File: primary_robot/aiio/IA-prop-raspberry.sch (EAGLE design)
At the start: 60 parts, among them U1 ARDUINO_R3_SHIELD

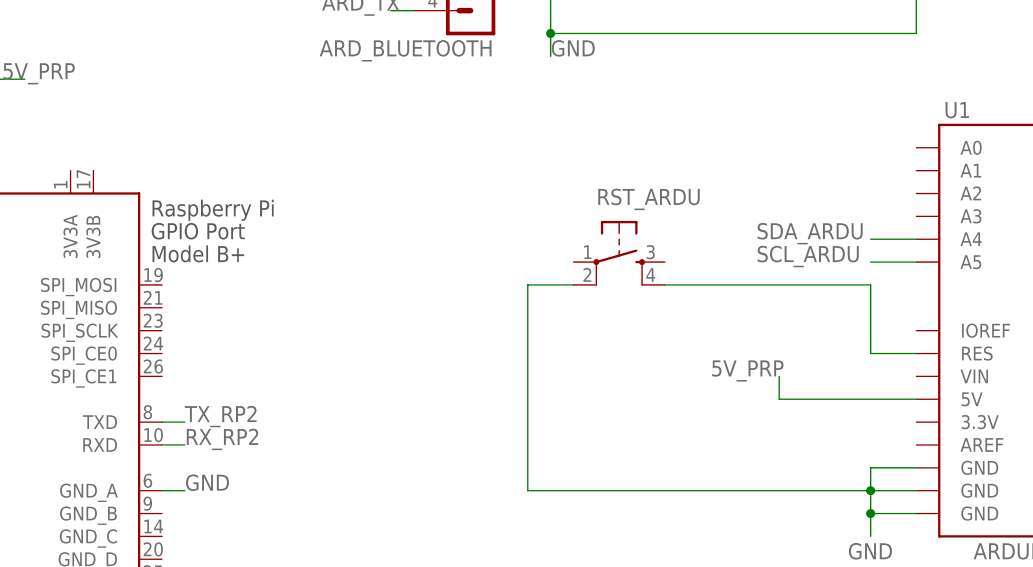
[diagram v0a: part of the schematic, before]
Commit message: [AIIO] Adds a reset button for the Raspi
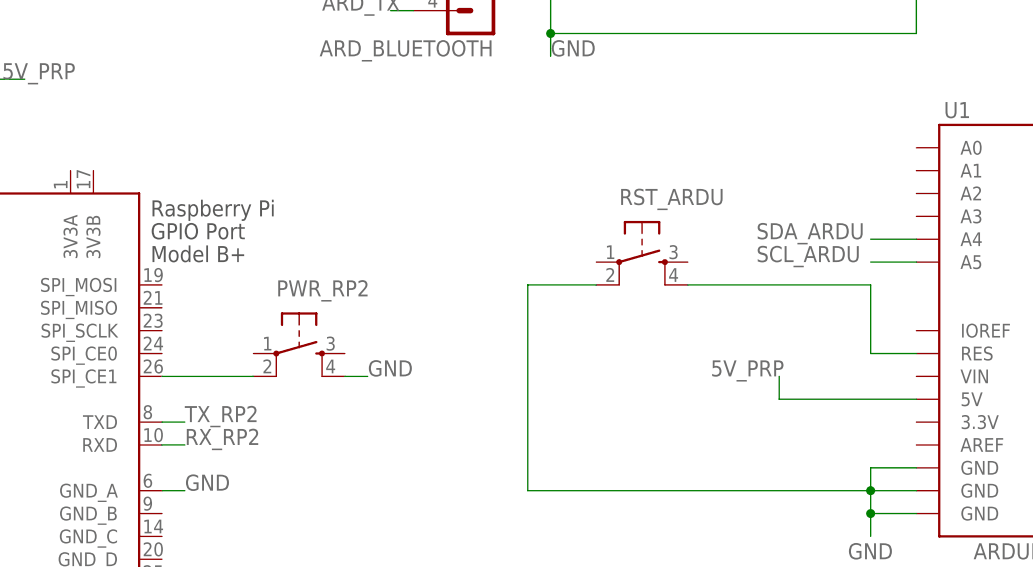
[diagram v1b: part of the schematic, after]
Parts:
- added PWR_RP2: (no value), SparkFun:TAC_SWITCHPTH
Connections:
- new net RP2_PWR: PWR_RP2.2, RP2.SPI_CE1
- net GND: now also PWR_RP2.4
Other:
- moved on the sheet: RST_ARDU
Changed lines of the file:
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@@
 <part name="R17" library="SparkFun" deviceset="RESISTOR" device="AXIAL-0.3" value="10K"/>
 <part name="R18" library="SparkFun" deviceset="RESISTOR" device="AXIAL-0.3" value="10K"/>
+<part name="PWR_RP2" library="SparkFun" deviceset="TAC_SWITCH" device="PTH"/>
 </parts>
 <sheets>
@@
 <instance part="LED1" gate="G$1" x="91.44" y="-83.82" rot="R180"/>
 <instance part="R3" gate="G$1" x="91.44" y="-71.12" rot="R90"/>
-<instance part="RST_ARDU" gate="S" x="165.1" y="-111.76"/>
+<instance part="RST_ARDU" gate="S" x="167.64" y="-111.76"/>
 <instance part="5V_SAL" gate="-1" x="-58.42" y="60.96"/>
 <instance part="5V_SAL" gate="-2" x="-58.42" y="55.88"/>
@@
 <instance part="R17" gate="G$1" x="-12.7" y="-63.5" rot="R90"/>
 <instance part="R18" gate="G$1" x="-12.7" y="-81.28" rot="R90"/>
+<instance part="PWR_RP2" gate="S" x="129.54" y="-121.92"/>
 </instances>
 <busses>
@@
 <label x="190.5" y="-144.78" size="1.778" layer="95"/>
 <pinref part="RST_ARDU" gate="S" pin="2"/>
-<wire x1="160.02" y1="-114.3" x2="154.94" y2="-114.3" width="0.1524" layer="91"/>
+<wire x1="162.56" y1="-114.3" x2="154.94" y2="-114.3" width="0.1524" layer="91"/>
 <wire x1="154.94" y1="-114.3" x2="154.94" y2="-137.16" width="0.1524" layer="91"/>
 <wire x1="154.94" y1="-137.16" x2="193.04" y2="-137.16" width="0.1524" layer="91"/>
@@
 <junction x="91.44" y="10.16"/>
 <label x="91.44" y="-2.54" size="1.778" layer="95"/>
+</segment>
+<segment>
+<pinref part="PWR_RP2" gate="S" pin="4"/>
+<wire x1="134.62" y1="-124.46" x2="137.16" y2="-124.46" width="0.1524" layer="91"/>
+<label x="137.16" y="-124.46" size="1.778" layer="95"/>
 </segment>
 </net>
@@
 <wire x1="198.12" y1="-121.92" x2="193.04" y2="-121.92" width="0.1524" layer="91"/>
 <pinref part="RST_ARDU" gate="S" pin="4"/>
-<wire x1="170.18" y1="-114.3" x2="193.04" y2="-114.3" width="0.1524" layer="91"/>
+<wire x1="172.72" y1="-114.3" x2="193.04" y2="-114.3" width="0.1524" layer="91"/>
 <wire x1="193.04" y1="-114.3" x2="193.04" y2="-121.92" width="0.1524" layer="91"/>
 </segment>
@@
 </segment>
 </net>
+<net name="RP2_PWR" class="0">
+<segment>
+<pinref part="RP2" gate="G$1" pin="SPI_CE1"/>
+<pinref part="PWR_RP2" gate="S" pin="2"/>
+<wire x1="114.3" y1="-124.46" x2="124.46" y2="-124.46" width="0.1524" layer="91"/>
+</segment>
+</net>

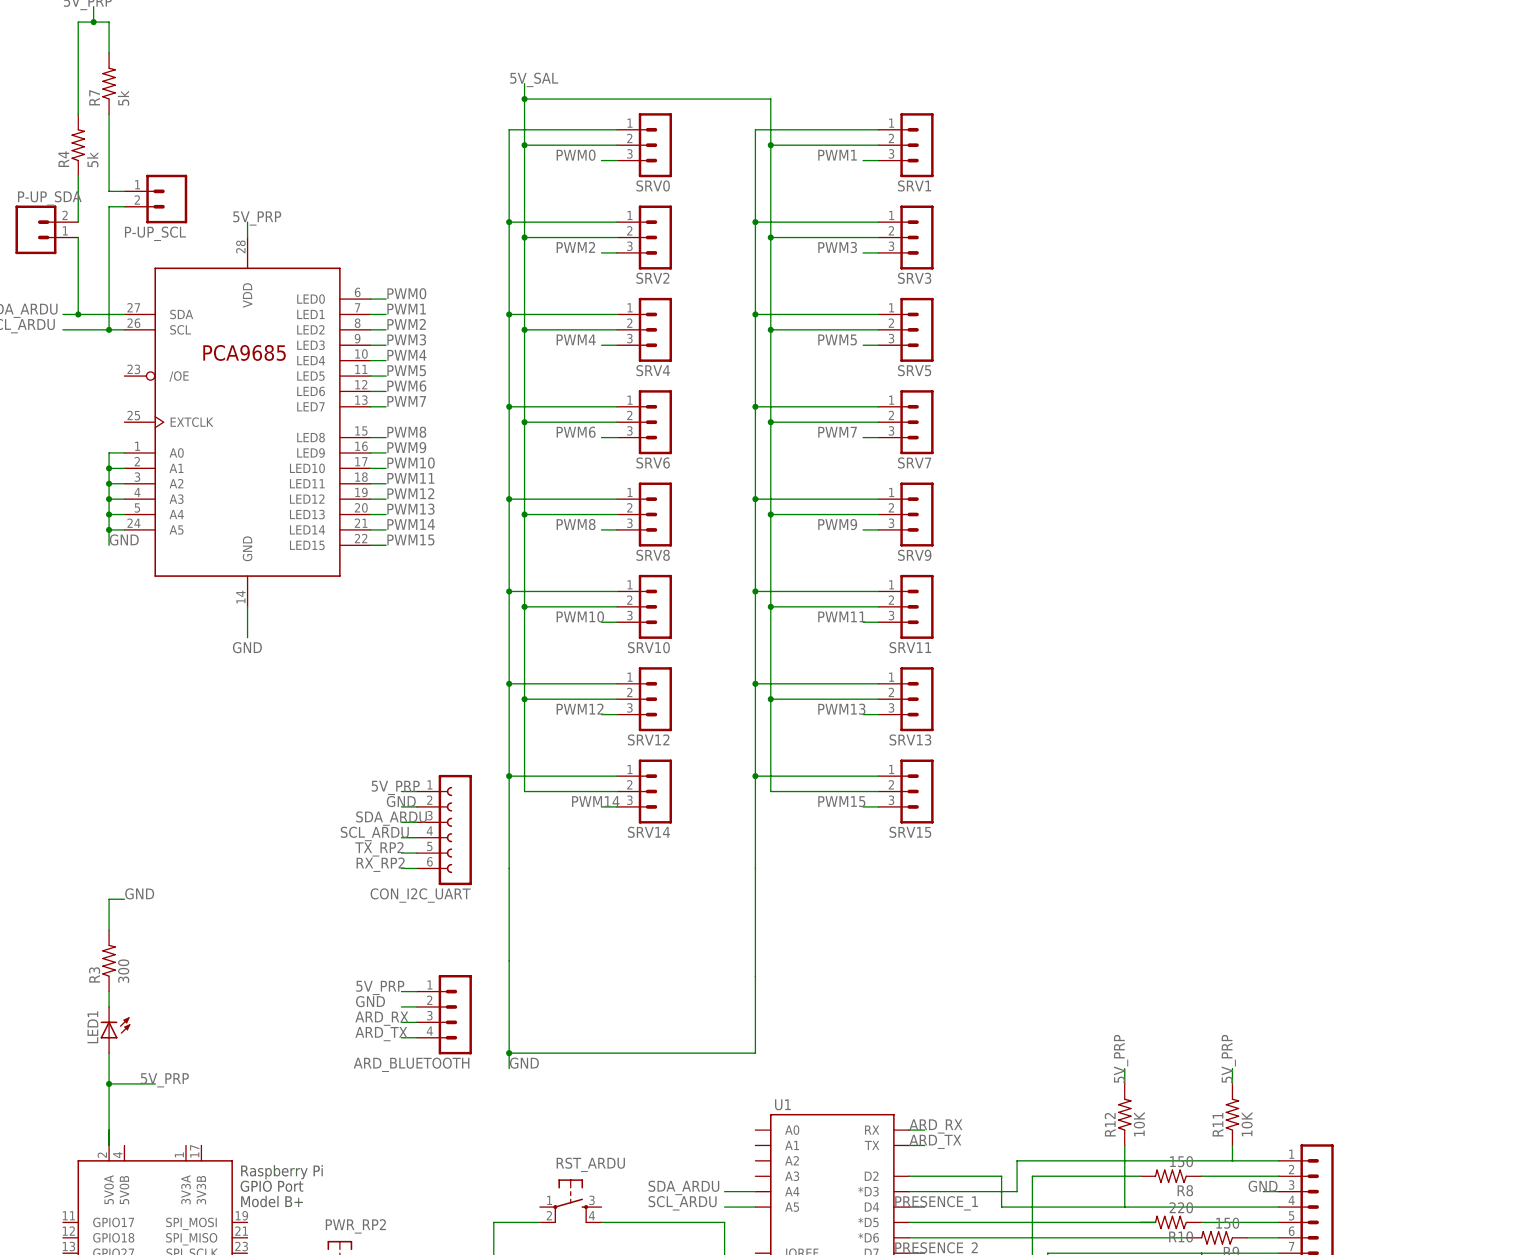
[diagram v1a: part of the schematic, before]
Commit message: [AIIO_board] Add I2C bus "I2C0" for sonar sensors on shematic file.
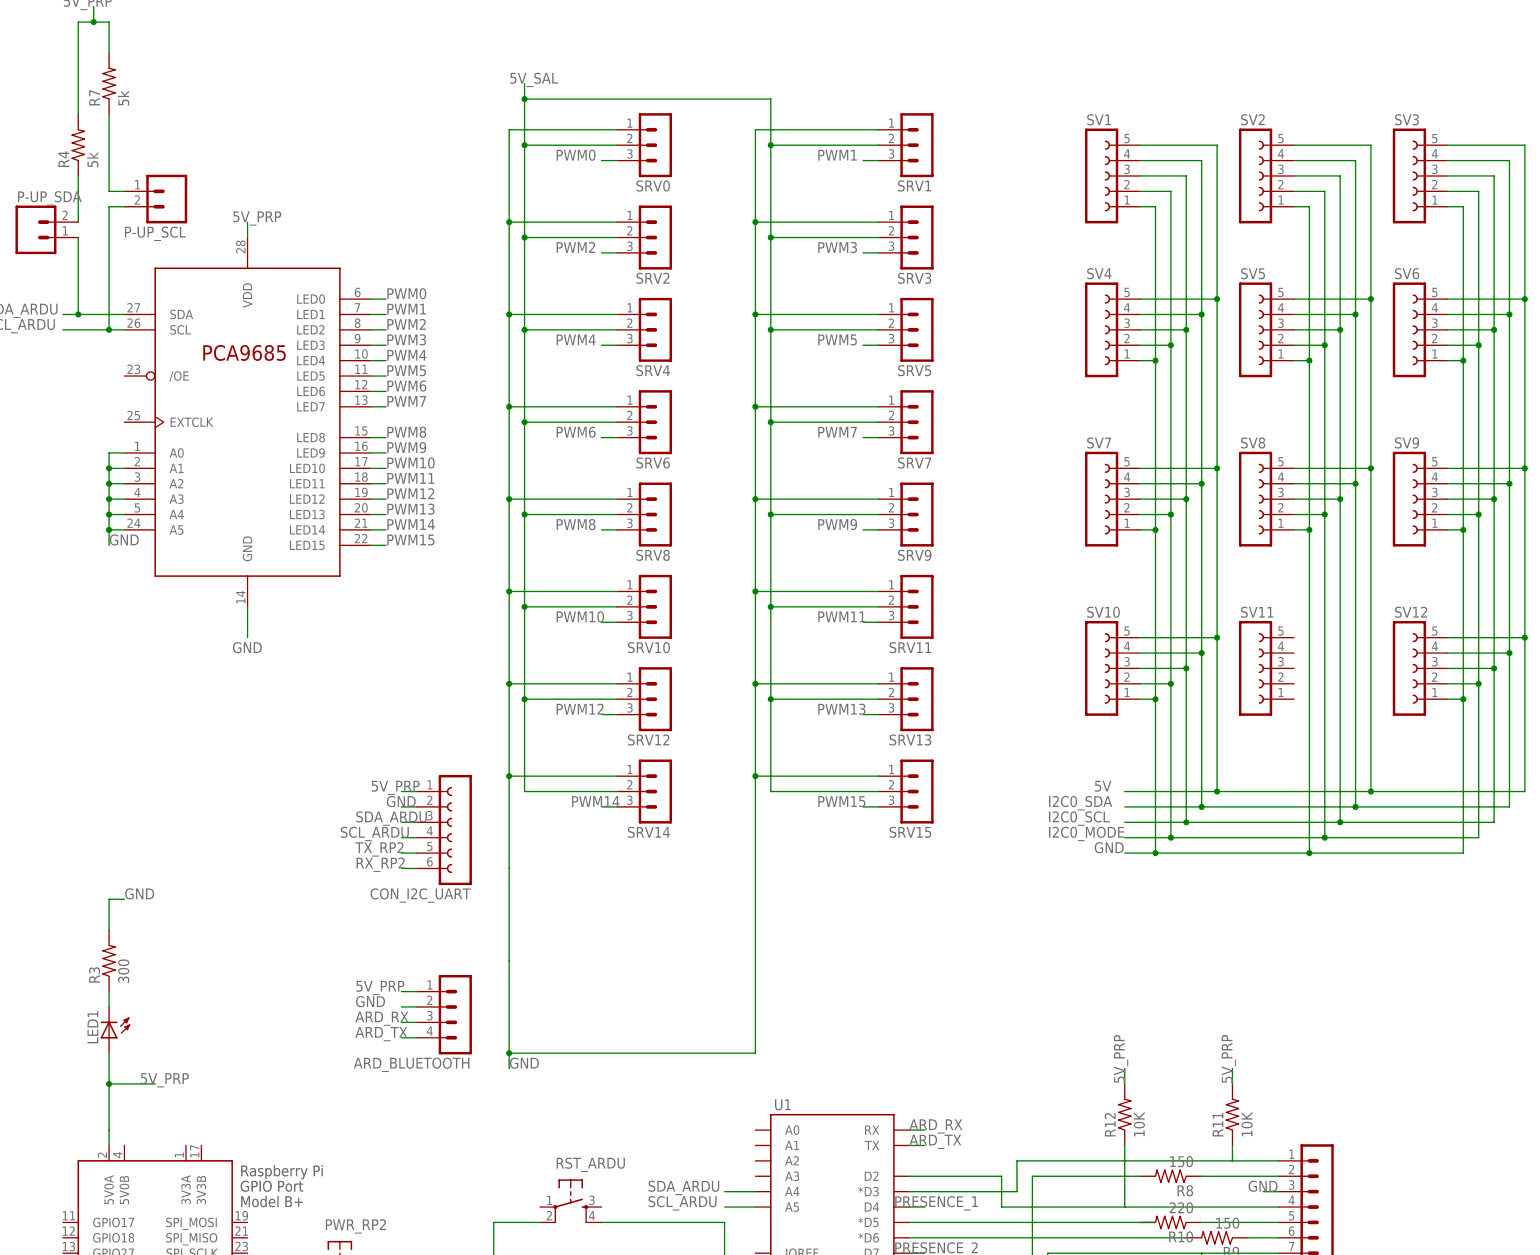
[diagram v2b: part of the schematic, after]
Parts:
- added SV1, SV10, SV11, SV12, SV2, SV3, SV4, SV5, SV6, SV7, SV8, SV9: (no value), con-lsta:FE05-1
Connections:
- new net 5V: SV1.5, SV10.5, SV12.5, SV2.5, SV3.5, SV4.5, SV5.5, SV6.5, SV7.5, SV8.5, SV9.5
- new net I2C0_MODE: SV1.2, SV10.2, SV12.2, SV2.2, SV3.2, SV4.2, SV5.2, SV6.2, SV7.2, SV8.2, SV9.2
- new net I2C0_SCL: SV1.3, SV10.3, SV12.3, SV2.3, SV3.3, SV4.3, SV5.3, SV6.3, SV7.3, SV8.3, SV9.3
- new net I2C0_SDA: SV1.4, SV10.4, SV12.4, SV2.4, SV3.4, SV4.4, SV5.4, SV6.4, SV7.4, SV8.4, SV9.4
- net GND: now also SV1.1, SV10.1, SV12.1, SV2.1, SV3.1, SV4.1, SV5.1, SV6.1, SV7.1, SV8.1, SV9.1
